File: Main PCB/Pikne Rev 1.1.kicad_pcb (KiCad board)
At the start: 4 copper layers, 60 x 30 mm, 111 parts, among them J1 USB_C_Receptacle_PowerOnly_6P, J2 bat, J3 Conn_01x03_Pin, J4 i2c, J6 program, SW1 SW_Push, SW2 SW_Push, U1 BQ25792RQMR, U2 ATmega328P-A, U3 OLED 0.91 inch, U4 PTPS25751DREFR, U5 TVS2200DRV, U6 TPS54531DDAR, U7 TLV75533PDBV, U8 CAT24C256, U9 TPS259461ARPW

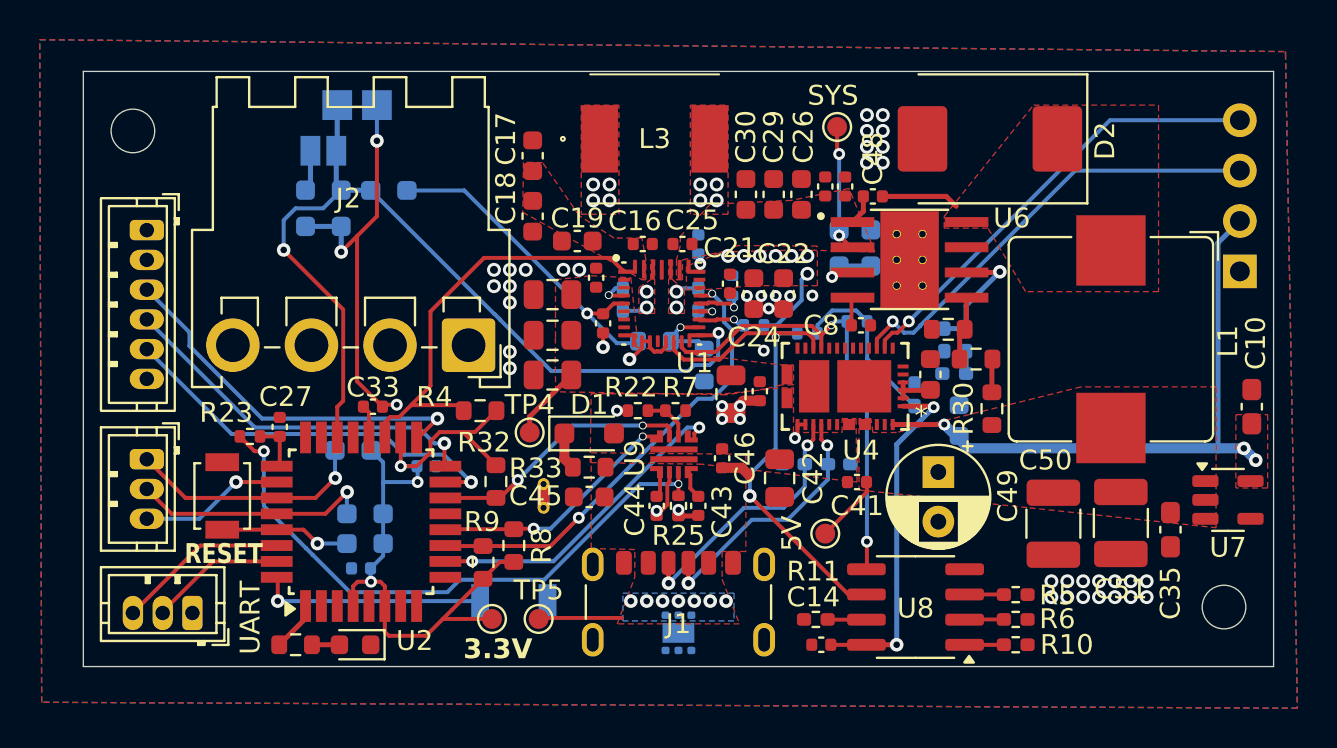
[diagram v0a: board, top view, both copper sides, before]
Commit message: Added BOMs and updated some PCB files
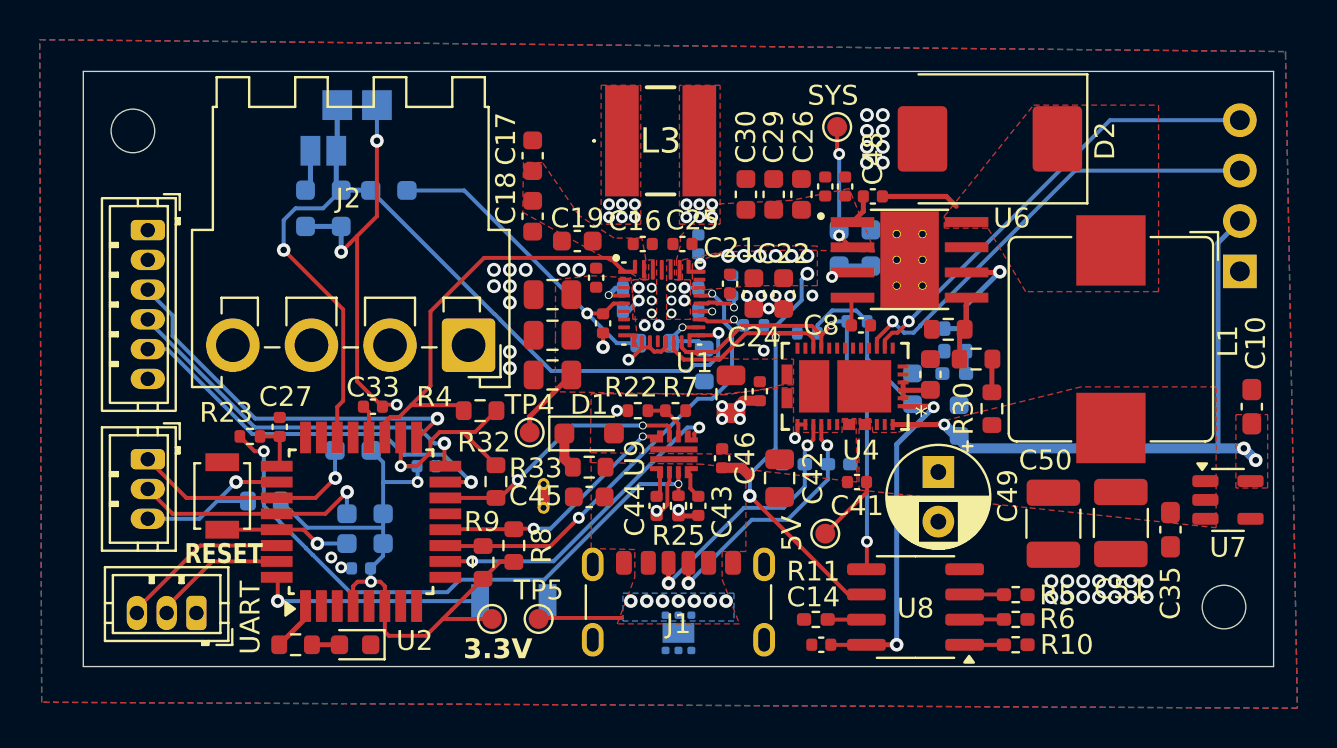
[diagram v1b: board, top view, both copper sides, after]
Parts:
- added R26: 4.7k, Resistor_SMD:R_0603_1608Metric, B.Cu at (121.1, 86.7)
- C36: footprint Capacitor_SMD:C_0402_1005Metric_Pad0.74x0.62mm_HandSolder -> Capacitor_SMD:C_0603_1608Metric
- L3: footprint SPM6550:SPM6550 -> Inductor:7443845030010
- moved C36 0.32 mm to (153.8, 81.0)
- moved L3 0.32 mm to (141.1, 68.5)
- moved J3 0.20 mm to (117.7, 92.3)
- moved R14 0.10 mm to (140.8, 78.7)
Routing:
- net /SW1: track 8.02 -> 1.01 mm, vias 6 -> 11
- net /SW2: track 7.63 -> 0.75 mm, vias 6 -> 11
- net +3V3: track 95.3 -> 101.0 mm
- net /alert: track 7.32 -> 8.87 mm
- net -BATT: vias 46 -> 50
